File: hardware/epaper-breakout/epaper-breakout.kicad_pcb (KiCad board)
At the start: 2 copper layers, 88 x 59 mm, 109 parts, among them J2 USB_C_16P, J3 Conn_02x06_Counter_Clockwise, Q1 AO3401A, Q2 AO3401A, Q3 MMBT3904, Q4 MMBT3904, Q5 AO3401A, Q6 MMBT3904, Q7 2N7002, SW1 SW_DIP_x01, U1 MCP1700-3302E_SOT23, U10 FPC-TOUCH, U11 TP4056, U12 CH340C, U13 CONN-Battery, U14 PCF8563T, U2 LT1945, U3 LT1945, U4 XC6206PxxxMR, U5 ESP32-WROVER, U6 ED060XC5, U7 LM358, U8 74HC4094-normal, U9 MCP9700AT-ETT, Y1 Crystal

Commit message: change outline
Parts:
- removed the H3 at (47.5, 28.4)
- removed the H4 at (85.6, 28.7)
- removed the R3 at (96.3, 80.4)
- added R14: 1k, Resistor_SMD:R_0805_2012Metric, F.Cu at (95.7, 82.0)
- moved TP1 6.28 mm to (83.2, 34.1)
- moved SW1 3.94 mm to (60.5, 25.7)
- moved J1 3.21 mm to (72.8, 28.1)
- renumbered C8 to C10, C9 to C12, C19 to C13, C12 to C14, C20 to C15, C21 to C16, C15 to C17, C17 to C18, C18 to C19, C6 to C2, C2 to C20, C24 to C21, C25 to C22, C22 to C23, C3 to C24, C26 to C25, C27 to C26, C23 to C27, C13 to C3, C7 to C5, C5 to C6, C10 to C7, C14 to C8, C16 to C9, D9 to D10, D4 to D2, D2 to D3, D5 to D4, D3 to D5, D10 to D8, D8 to D9, H5 to H3, H6 to H4, J2 to J1, J3 to J2, Q3 to Q2, Q4 to Q3, Q6 to Q4, Q7 to Q5, Q2 to Q6, Q5 to Q7, R23 to R1, R19 to R10, R14 to R11, R10 to R12, R2 to R13, R8 to R15, R9 to R16, R13 to R17, R1 to R18, R11 to R19, R24 to R2, R15 to R20, R25 to R23, R12 to R24, R26 to R25, R27 to R26, R20 to R27, R4 to R3, R5 to R4, R16 to R5, R17 to R6, R6 to R7, R7 to R8, R18 to R9, U2 to U1, U5 to U10, U14 to U11, U9 to U12, U6 to U13, U10 to U14, U3 to U2, U4 to U3, U12 to U4, U8 to U5, U7 to U6, U13 to U7, U11 to U8, U1 to U9
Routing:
- net GND: track 149.3 -> 140.7 mm, vias 25 -> 27
- net Net-(C20-Pad2): track 64.9 -> 69.7 mm
- net VIN: track 146.9 -> 151.1 mm
- net Net-(J1-PadA5): track 19.2 -> 23.0 mm
- net /USB_D+: track 10.8 -> 14.4 mm
- net /USB_D-: track 9.42 -> 12.7 mm
- net /EP_VCOM: track 31.4 -> 28.4 mm, vias 2 -> 0
- net Net-(J1-PadB5): track 15.7 -> 17.7 mm
- net Net-(D9-Pad1): track 6.44 -> 4.79 mm
- net Net-(R14-Pad1): track 19.0 -> 20.5 mm
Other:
- board size 88 x 59 mm -> 88 x 62 mm

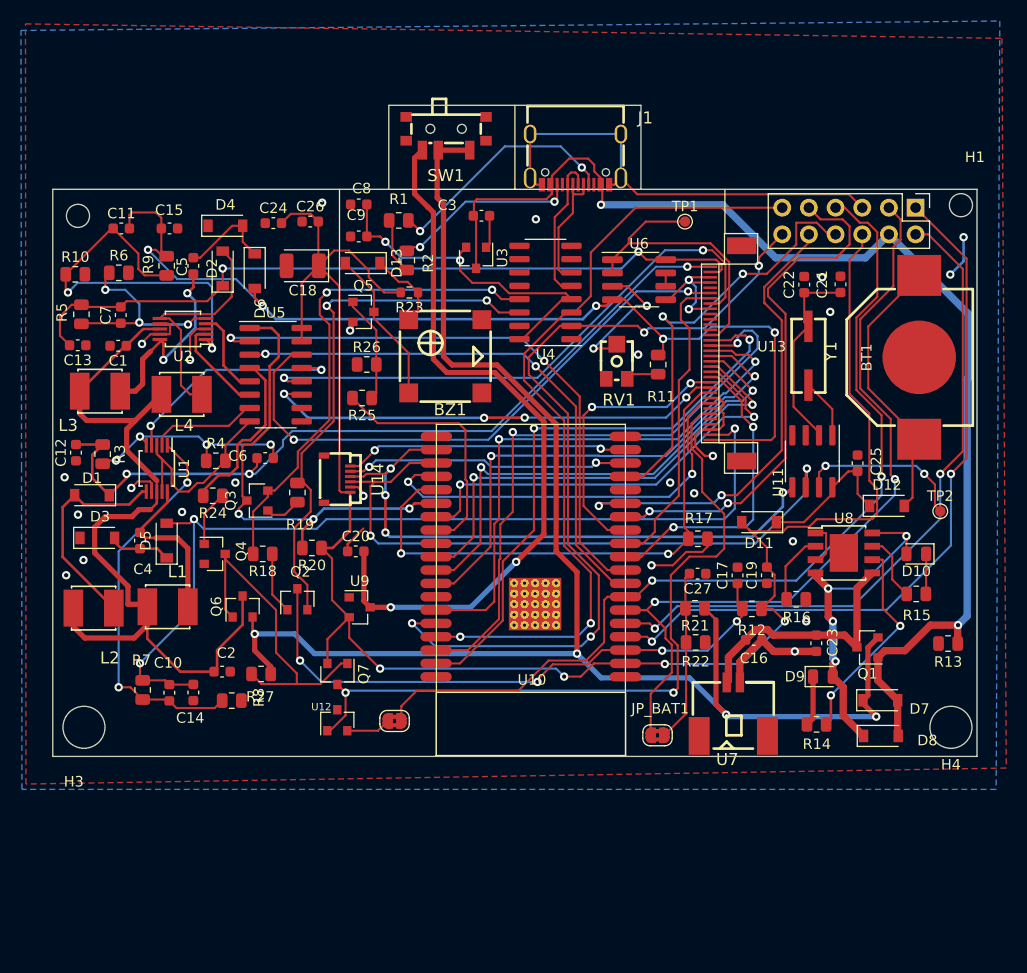
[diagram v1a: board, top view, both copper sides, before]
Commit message: Re-position connector
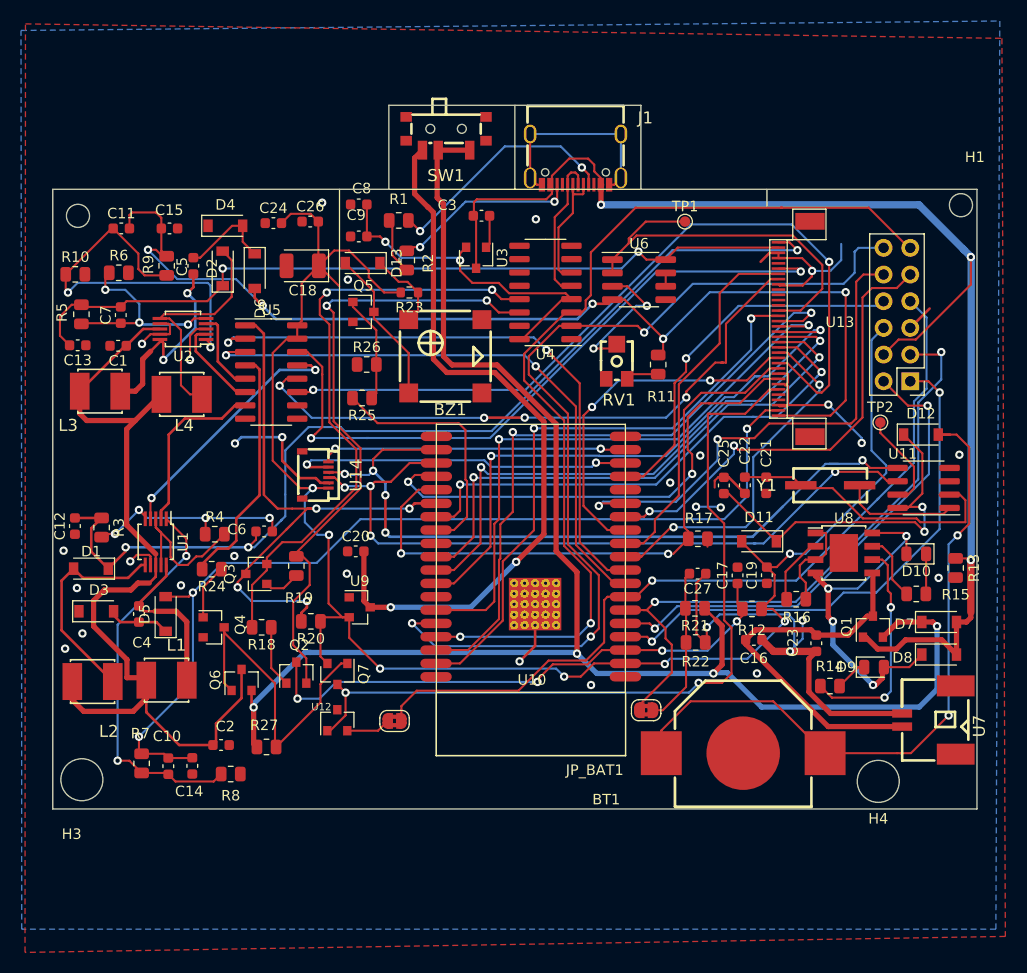
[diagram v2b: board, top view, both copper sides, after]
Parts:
- moved BT1 41.2 mm to (88.7, 84.7), turned to 180 degrees
- moved C21 20.4 mm to (90.9, 59.2), turned to 270 degrees
- moved C22 19.9 mm to (88.9, 59.2), turned to 270 degrees
- moved U7 18.7 mm to (106.4, 81.5), turned to 90 degrees
- moved J2 16.5 mm to (104.6, 49.3), turned to 180 degrees
- moved C25 12.9 mm to (86.9, 59.2)
- moved Y1 12.5 mm to (97.0, 59.2), turned to 180 degrees
- moved U11 10.9 mm to (105.9, 59.4), turned to 180 degrees
- moved TP2 10.2 mm to (101.8, 53.2)
- moved D8 9.53 mm to (107.4, 75.3)
- moved D7 9.32 mm to (107.4, 72.2)
- moved H4 8.63 mm to (101.6, 87.4)
- moved D12 7.52 mm to (105.7, 54.4)
- moved R13 7.23 mm to (109.0, 67.1), turned to 90 degrees
- moved C10 6.99 mm to (34.0, 85.9)
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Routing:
- net Net-(BT1-Pad1): track 26.6 -> 65.8 mm, vias 0 -> 2
- net /EP_OE: track 44.7 -> 76.8 mm, vias 4 -> 2
- net GND: track 140.7 -> 168.1 mm, vias 27 -> 30
- net Net-(C25-Pad2): track 13.9 -> 36.2 mm, vias 0 -> 2
- net /SENSOR_VP: track 69.8 -> 50.9 mm
- net /SENSOR_VN: track 65.1 -> 46.9 mm
- net /+22V: track 77.0 -> 94.9 mm
- net /TCH_SDA: track 57.2 -> 71.9 mm, vias 4 -> 5
- net /USB_RXD: track 77.2 -> 91.5 mm
- net /A0: track 75.1 -> 61.4 mm
- net /IO0: track 45.2 -> 57.3 mm, vias 3 -> 4
- net VBUS: track 116.6 -> 128.6 mm, vias 2 -> 3
- net BAT+: track 24.2 -> 36.2 mm
- net /A1: track 89.8 -> 78.9 mm, vias 2 -> 1
- net /+3.3V: track 171.6 -> 161.1 mm, vias 4 -> 7
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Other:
- board size 88 x 62 mm -> 88 x 67 mm
